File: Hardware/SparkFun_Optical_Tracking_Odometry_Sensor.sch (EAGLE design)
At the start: 41 parts, among them J1 QWIIC_RIGHT_ANGLE, J2 QWIIC_RIGHT_ANGLE, U1 PAA5160, U2 LSM6DS0, U3 STM32C011F4U6, U4 RT9080-33GJ5

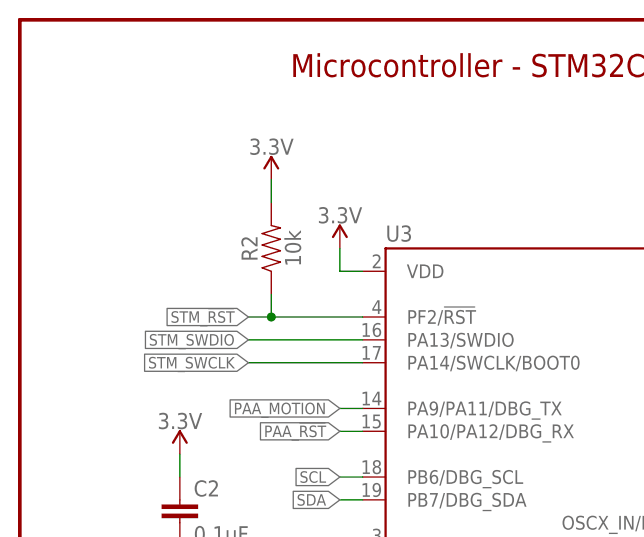
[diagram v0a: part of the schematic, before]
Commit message: PAA5160 footprint tweaks
Adjust pads to match datasheet recommendations
Reduce silk outline to be only in corners
Add tDocu lines for sensor location and pin 1 indication

Also remove pullup resistor on the STM reset net, the STM has an internal pullup
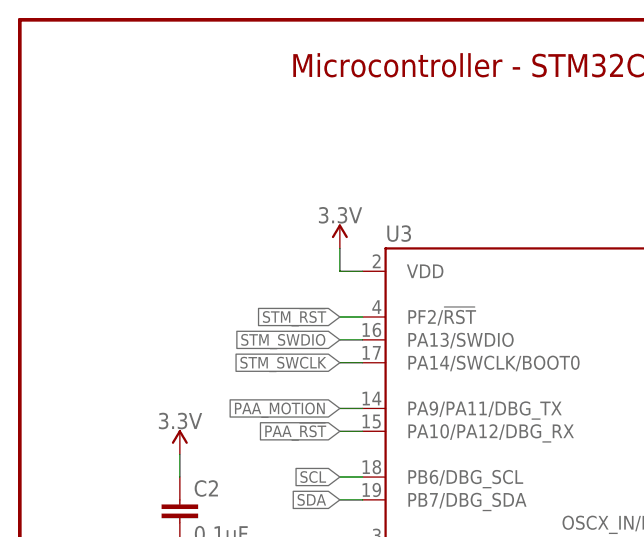
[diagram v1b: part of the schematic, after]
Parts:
- removed R2: 10k, SparkFun-Resistors:10KOHM-0603-1/10W-1%
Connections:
- net 3.3V: no longer R2.2
- net STM_!RST!: no longer R2.1
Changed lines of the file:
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@@
 <part name="SUPPLY10" library="SparkFun-PowerSymbols" deviceset="3.3V" device=""/>
 <part name="GND8" library="SparkFun-PowerSymbols" deviceset="GND" device=""/>
-<part name="R2" library="SparkFun-Resistors" deviceset="10KOHM" device="-0603-1/10W-1%" value="10k"/>
-<part name="SUPPLY11" library="SparkFun-PowerSymbols" deviceset="3.3V" device=""/>
 <part name="U$1" library="SparkFun-Connectors" deviceset="SWD-5PIN" device=""/>
 <part name="SUPPLY12" library="SparkFun-PowerSymbols" deviceset="3.3V" device=""/>
@@
 <attribute name="VALUE" x="124.46" y="81.026" size="1.778" layer="96" font="vector" align="top-center"/>
 </instance>
-<instance part="R2" gate="G$1" x="27.94" y="160.02" smashed="yes" rot="R90">
-<attribute name="NAME" x="26.416" y="160.02" size="1.778" layer="95" font="vector" rot="R90" align="bottom-center"/>
-<attribute name="VALUE" x="29.464" y="160.02" size="1.778" layer="96" font="vector" rot="R90" align="top-center"/>
-</instance>
-<instance part="SUPPLY11" gate="G$1" x="27.94" y="167.64" smashed="yes">
-<attribute name="VALUE" x="27.94" y="170.434" size="1.778" layer="96" font="vector" align="bottom-center"/>
-</instance>
 <instance part="U$1" gate="G$1" x="218.44" y="165.1" smashed="yes">
 <attribute name="NAME" x="214.884" y="170.688" size="1.778" layer="95" font="vector"/>
@@
 </segment>
 <segment>
-<pinref part="SUPPLY11" gate="G$1" pin="3.3V"/>
-<pinref part="R2" gate="G$1" pin="2"/>
-<wire x1="27.94" y1="167.64" x2="27.94" y2="165.1" width="0.1524" layer="91"/>
-</segment>
-<segment>
 <pinref part="U$1" gate="G$1" pin="1"/>
 <pinref part="SUPPLY12" gate="G$1" pin="3.3V"/>
@@
 <segment>
 <pinref part="U3" gate="G$1" pin="PF2/!RST!"/>
-<pinref part="R2" gate="G$1" pin="1"/>
-<wire x1="38.1" y1="152.4" x2="27.94" y2="152.4" width="0.1524" layer="91"/>
-<wire x1="27.94" y1="152.4" x2="27.94" y2="154.94" width="0.1524" layer="91"/>
-<wire x1="27.94" y1="152.4" x2="25.4" y2="152.4" width="0.1524" layer="91"/>
-<junction x="27.94" y="152.4"/>
-<label x="25.4" y="152.4" size="1.27" layer="95" font="vector" rot="R180" xref="yes"/>
+<wire x1="38.1" y1="152.4" x2="35.56" y2="152.4" width="0.1524" layer="91"/>
+<label x="35.56" y="152.4" size="1.27" layer="95" font="vector" rot="R180" xref="yes"/>
 </segment>
 <segment>
@@
 <segment>
 <pinref part="U3" gate="G$1" pin="PA13/SWDIO"/>
-<wire x1="38.1" y1="149.86" x2="25.4" y2="149.86" width="0.1524" layer="91"/>
-<label x="25.4" y="149.86" size="1.27" layer="95" font="vector" rot="R180" xref="yes"/>
+<wire x1="38.1" y1="149.86" x2="35.56" y2="149.86" width="0.1524" layer="91"/>
+<label x="35.56" y="149.86" size="1.27" layer="95" font="vector" rot="R180" xref="yes"/>
 </segment>
 <segment>
@@
 <segment>
 <pinref part="U3" gate="G$1" pin="PA14/SWCLK/BOOT0"/>
-<wire x1="38.1" y1="147.32" x2="25.4" y2="147.32" width="0.1524" layer="91"/>
-<label x="25.4" y="147.32" size="1.27" layer="95" font="vector" rot="R180" xref="yes"/>
-</segment>
-<segment>
+<wire x1="38.1" y1="147.32" x2="35.56" y2="147.32" width="0.1524" layer="91"/>
+<label x="35.56" y="147.32" size="1.27" layer="95" font="vector" rot="R180" xref="yes"/>
+</segment>
+<segment>

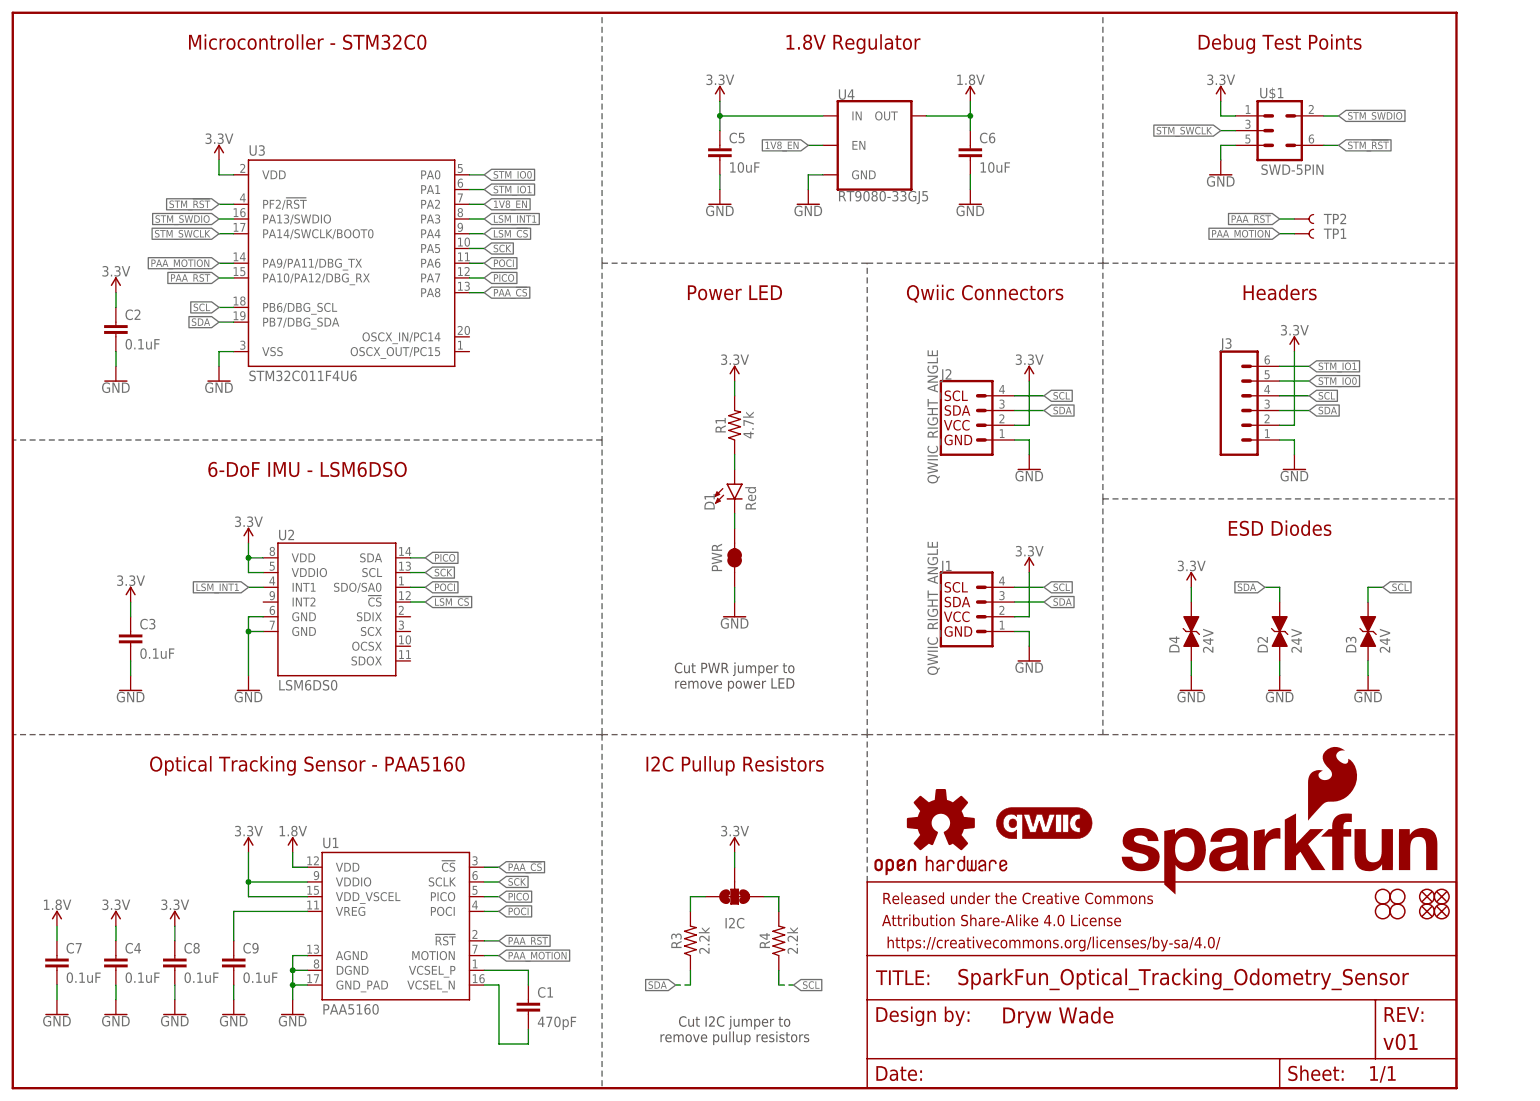
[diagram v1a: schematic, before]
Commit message: v02 update
Add MOSFETs controlled by GPIO pins in order to supply power to PAA5160 with correct timings
Add correct decoupling capacitors
Rearrange some GPIO pins
Reduce silk around STM32C0
Reroute entire board 🙃
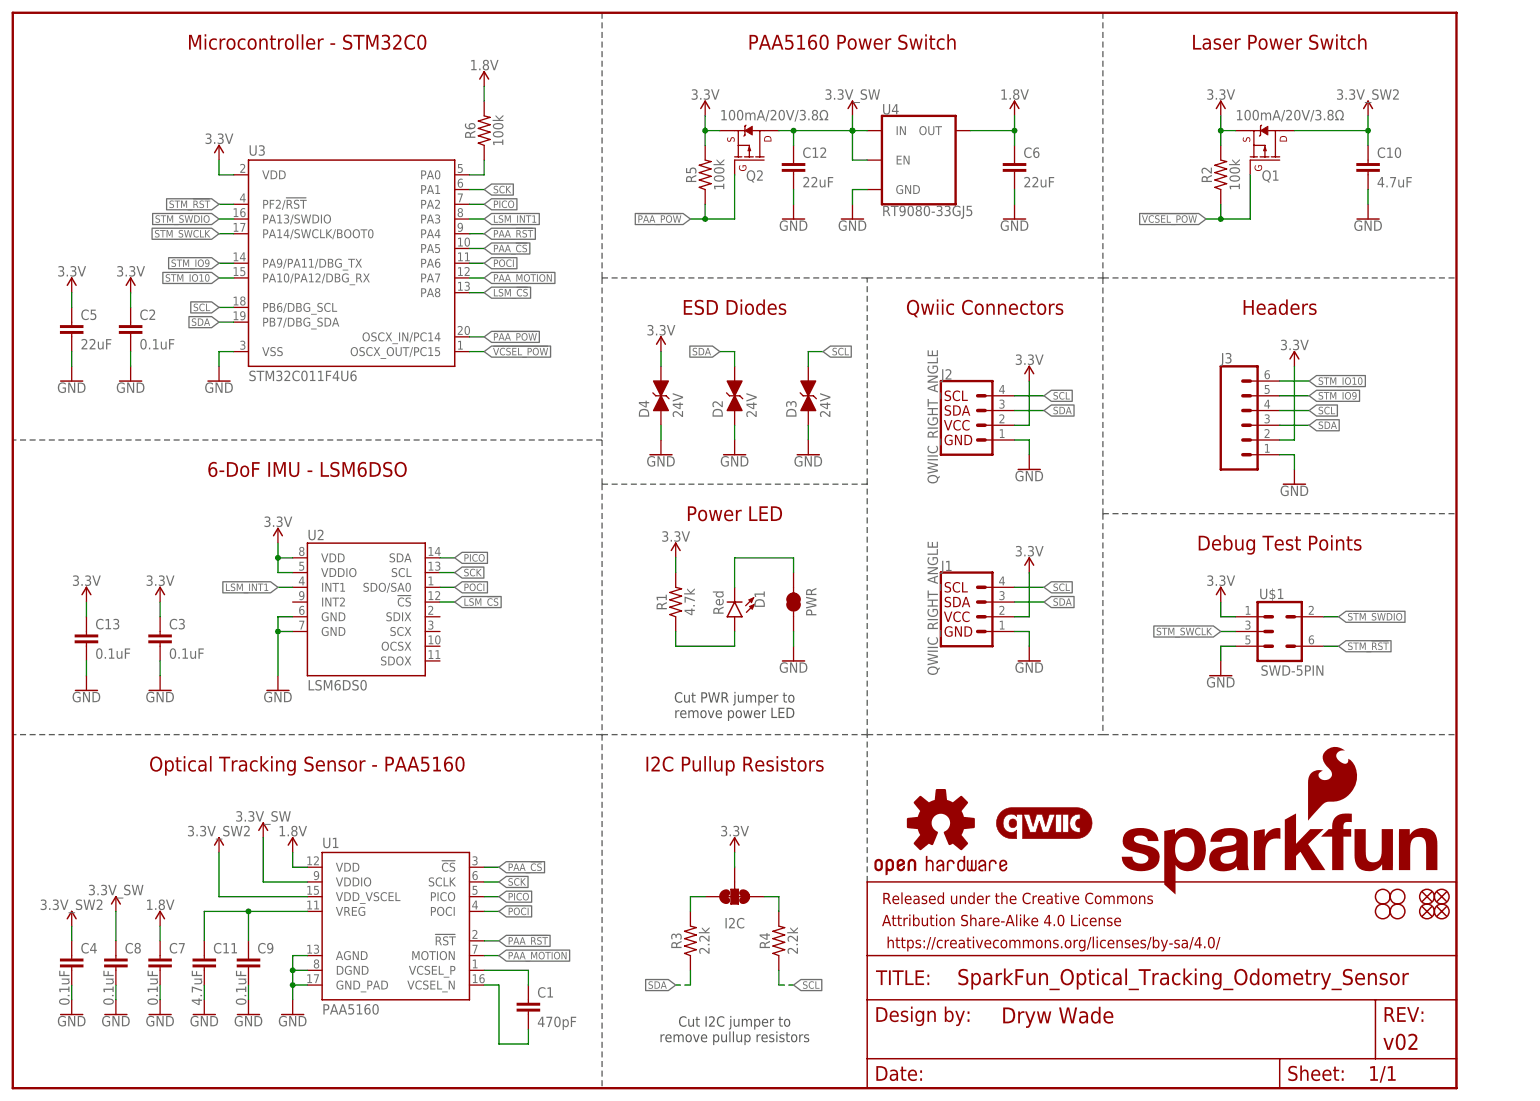
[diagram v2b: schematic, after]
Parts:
- removed TP1, TP2: TEST-POINT3X5, SparkFun-Connectors:TEST-POINT3X5
- added C10, C11: 4.7uF, SparkFun-Capacitors:4.7UF-0603-6.3V-(10%)
- added C12: 22uF, SparkFun-Capacitors:22UF-0603-6.3V-20%
- added C13: 0.1uF, SparkFun-Capacitors:0.1UF-0603-25V-(+80/-20%)
- added Q1, Q2: 100mA/20V/3.8Ω, SparkFun-DiscreteSemi:MOSFET_PCH-RE1C001ZPTL
- added R2, R5, R6: 100k, SparkFun-Resistors:100KOHM-0603-1/10W-1%
- C5, C6: value 10uF -> 22uF; device SparkFun-Capacitors:10UF-0603-6.3V-20% -> SparkFun-Capacitors:22UF-0603-6.3V-20%
- FRAME1: REV v01 -> v02
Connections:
- removed net 1V8_EN: U3.PA2, U4.EN
- removed net STM_IO0: J3.5, U3.PA0
- removed net STM_IO1: J3.6, U3.PA1
- new net !PAA_POW!: Q2.G, R5.1, U3.OSCX_IN/PC14
- new net !VCSEL_POW!: Q1.G, R2.1, U3.OSCX_OUT/PC15
- new net 3.3V_SW: C12.1, C8.1, Q2.D, U1.VDDIO, U4.EN, U4.IN
- new net 3.3V_SW2: C10.1, C4.1, Q1.D, U1.VDD_VSCEL
- new net N$8: R6.1, U3.PA0
- new net STM_IO10: J3.6, U3.PA10/PA12/DBG_RX
- new net STM_IO9: J3.5, U3.PA9/PA11/DBG_TX
- net 1.8V: now also R6.2
- net 3.3V: now also C13.1, Q1.S, Q2.S, R2.2, R5.2; no longer C4.1, C8.1, U1.VDDIO, U1.VDD_VSCEL, U4.IN
- net GND: now also C10.2, C11.2, C12.2, C13.2
- net LSM_!CS!: now also U3.PA8; no longer U3.PA4
- net N$7: now also C11.1
- net PAA_!CS!: now also U3.PA5; no longer U3.PA8
- net PAA_!RST!: now also U3.PA4; no longer TP2.1, U3.PA10/PA12/DBG_RX
- net PAA_MOTION: now also U3.PA7; no longer TP1.1, U3.PA9/PA11/DBG_TX
- net PICO: now also U3.PA2; no longer U3.PA7
- net SCK: now also U3.PA1; no longer U3.PA5
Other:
- note added: "Laser Power Switch"
- note added: "PAA5160 Power Switch"
- note removed: "1.8V Regulator"
- moved on the sheet: C2, C3, C4, C5, C6, C7, C8, C9, D1, D2, D3, D4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

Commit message: Design review updates
Add regulator name to section in schematic
Add voltage ranges for each component, and required voltage range for entire board
Add GND via next to STM32 GND pad
Center traces between Q1 and R2
Nudge via and 3.3V trace left of R6 to get better GND stitching
Fix acid trap with via under U4
Fix orientation of silk on bottom
Add silk line between D4 and C5
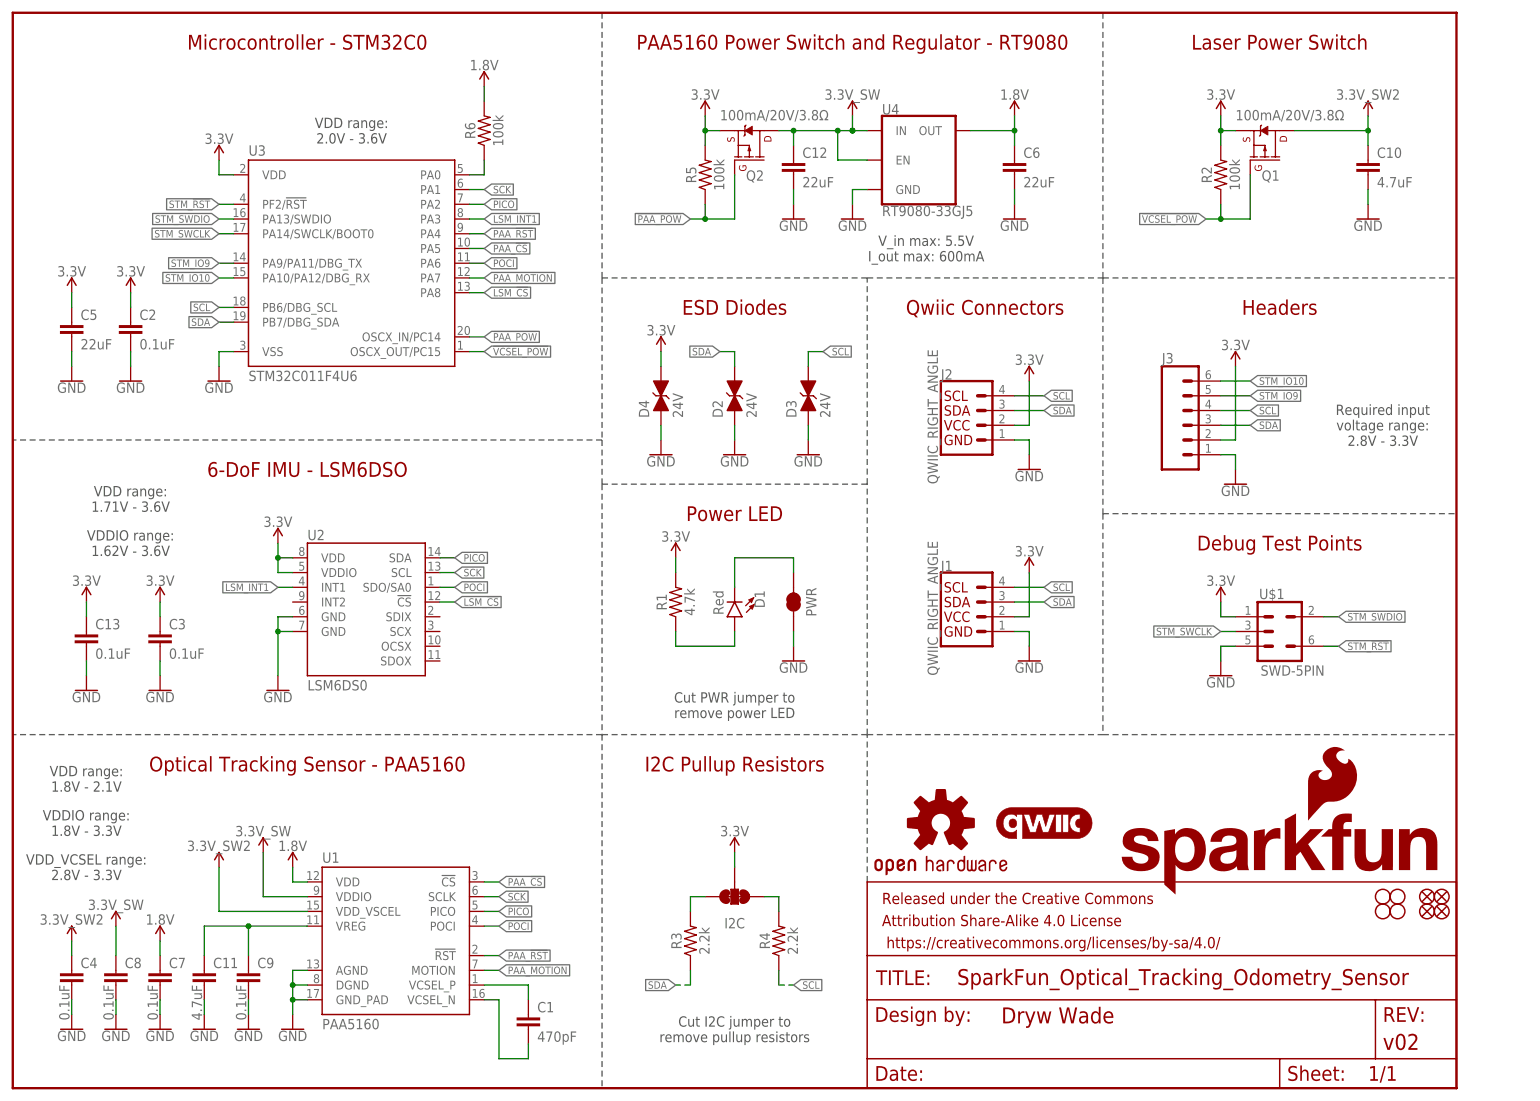
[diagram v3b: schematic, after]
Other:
- note added: "PAA5160 Power Switch and Regulator - RT9080"
- note added: "Required input voltage range: 2.8V - 3.3V"
- note added: "VDD range: 1.71V - 3.6V"
- note added: "VDD range: 1.8V - 2.1V"
- note added: "VDD range: 2.0V - 3.6V"
- note added: "VDDIO range: 1.62V - 3.6V"
- note added: "VDDIO range: 1.8V - 3.3V"
- note added: "VDD_VCSEL range: 2.8V - 3.3V"
- note added: "V_in max: 5.5V I_out max: 600mA"
- note removed: "PAA5160 Power Switch"
- moved on the sheet: C1, C11, C4, C7, C8, C9, J3, U1

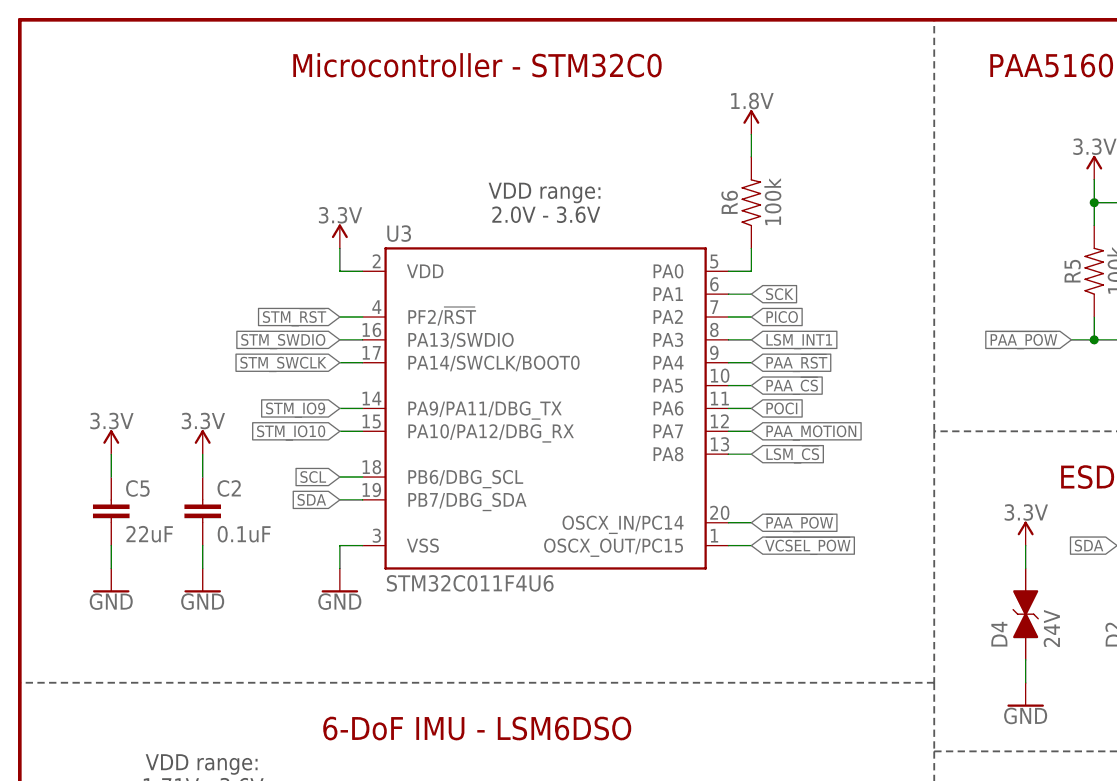
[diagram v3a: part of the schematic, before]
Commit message: Add pulldown resistor to BOOT0 pin
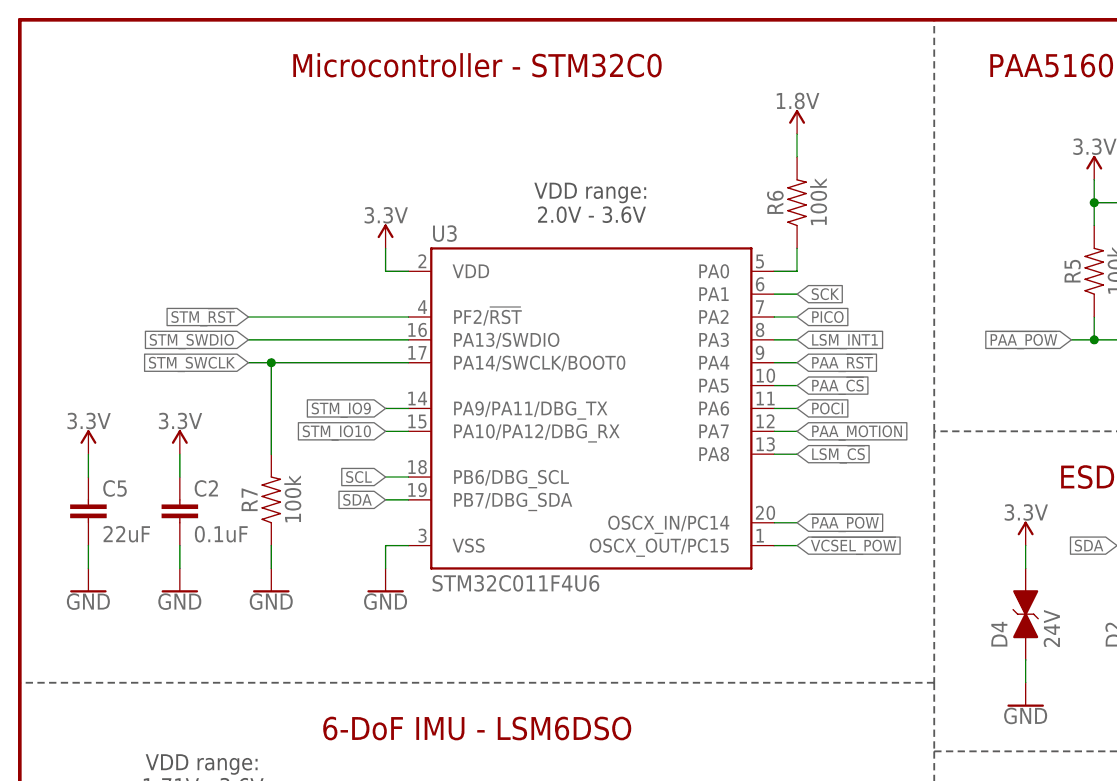
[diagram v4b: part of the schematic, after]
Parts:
- added R7: 100k, SparkFun-Resistors:100KOHM-0603-1/10W-1%
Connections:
- net GND: now also R7.1
- net STM_SWCLK: now also R7.2
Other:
- moved on the sheet: C2, C5, R6, U3
